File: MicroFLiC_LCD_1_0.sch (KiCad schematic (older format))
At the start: 14 parts, among them P1 CONN_01X01, P2 CONN_01X01, P3 CONN_01X16, Q1 BCX54-16, U1 MCP4728, U2 TLV2371

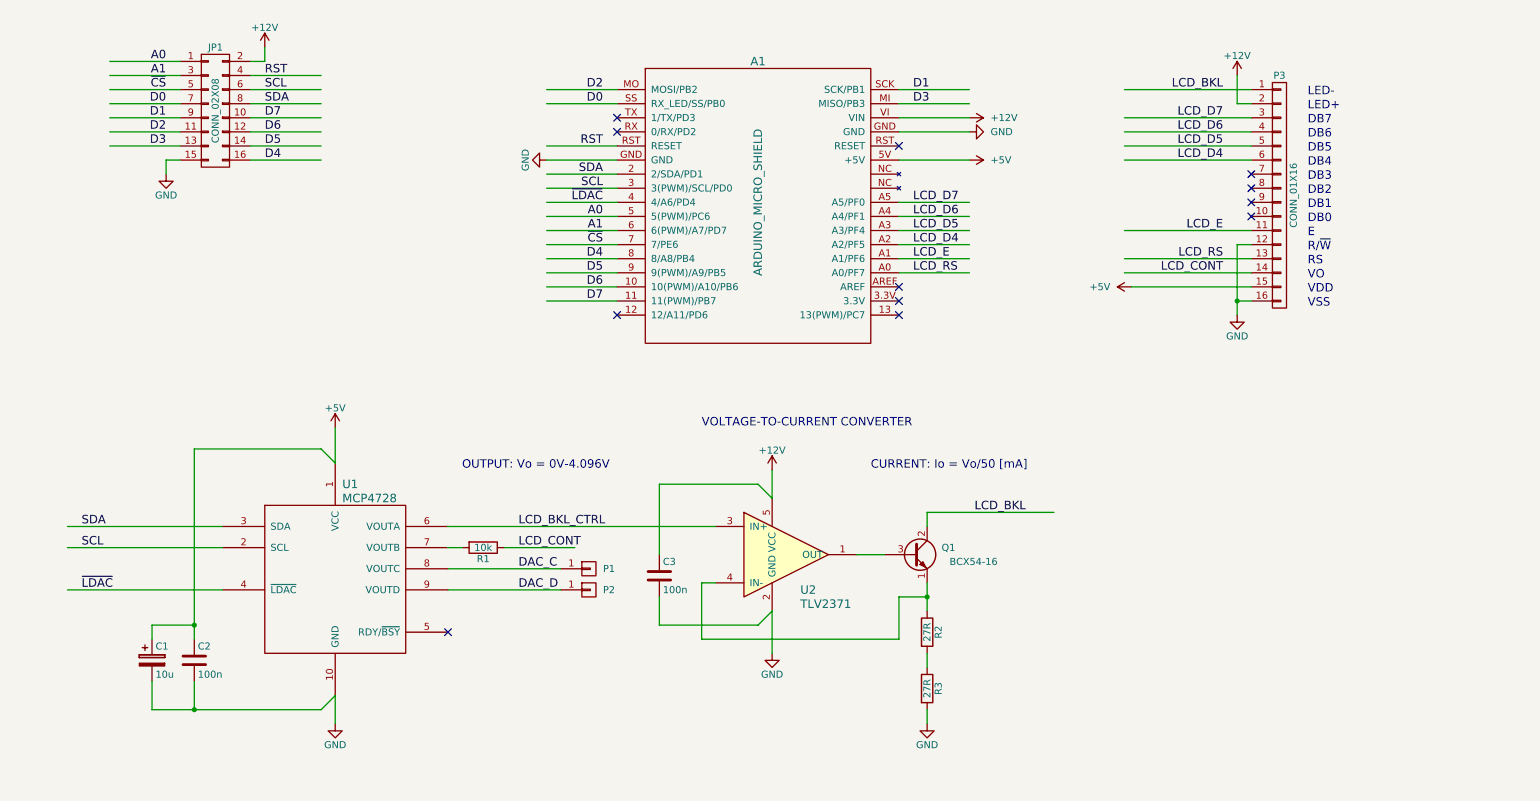
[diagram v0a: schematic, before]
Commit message: Created the PCB with 3D models
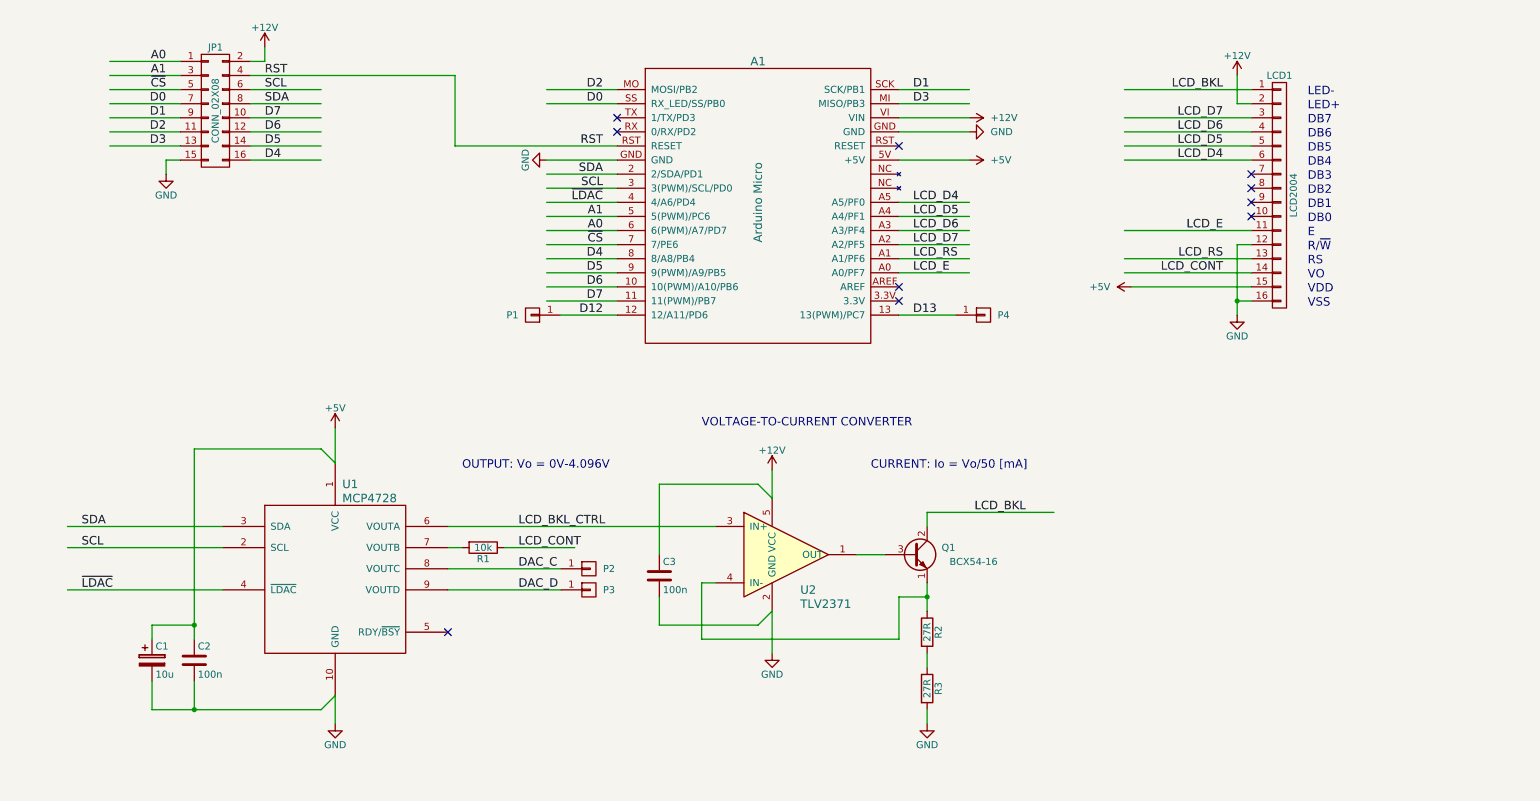
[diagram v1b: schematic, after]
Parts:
- added P1, P4: CONN_01X01, jakub:PIN_ARRAY_1, symbol CONN_01X01
- A1: value ARDUINO_MICRO_SHIELD -> Arduino Micro; footprint jakub:ARDUINO_MICRO_SHIELD -> jakub:ArduinoMicro
- JP1: footprint Socket_Strips:Socket_Strip_Straight_2x08 -> jakub:1-188275-6
- LCD1: renamed from P3; value CONN_01X16 -> LCD2004; footprint Socket_Strips:Socket_Strip_Straight_1x16 -> jakub:LCD2004
- Q1: footprint TO_SOT_Packages_SMD:SOT89-5_Housing -> TO_SOT_Packages_SMD:SOT89-3_Housing
- renumbered P1 to P2, P2 to P3
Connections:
- net labels added: D12, D13
- wire segments 95 -> 98
- no-connect marks 12 -> 10
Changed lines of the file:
@@
 P 6100 2300
 F 0 "A1" H 6100 3300 60  0000 C CNN
-F 1 "ARDUINO_MICRO_SHIELD" V 6100 2300 60  0000 C CNN
-F 2 "jakub:ARDUINO_MICRO_SHIELD" V 5350 2750 60  0001 C CNN
+F 1 "Arduino Micro" V 6100 2300 60  0000 C CNN
+F 2 "jakub:ArduinoMicro" V 5350 2750 60  0001 C CNN
 F 3 "" V 5350 2750 60  0000 C CNN
 	1    6100 2300
@@
 F 0 "JP1" H 2250 2100 50  0000 C CNN
 F 1 "CONN_02X08" V 2250 1650 50  0000 C CNN
-F 2 "Socket_Strips:Socket_Strip_Straight_2x08" H 2250 450 50  0001 C CNN
+F 2 "jakub:1-188275-6" H 2250 450 50  0001 C CNN
 F 3 "" H 2250 450 50  0000 C CNN
 	1    2250 1650
@@
 	2000 2000 1900 2000
 Wire Wire Line
-	3000 1400 2500 1400
+	2500 1400 3950 1400
 Text Label 2600 1400 0    60   ~ 0
 RST
@@
 $EndComp
 Wire Wire Line
-	5100 1900 4600 1900
+	3950 1900 5100 1900
 Text Label 5000 1900 2    60   ~ 0
 RST
@@
 D6
 Wire Wire Line
+	5100 2500 4600 2500
+Text Label 5000 2500 2    60   ~ 0
+A0
+Wire Wire Line
 	5100 2600 4600 2600
+Wire Wire Line
+	5100 2400 4600 2400
 Text Label 5000 2600 2    60   ~ 0
 ~CS
-Wire Wire Line
-	5100 2400 4600 2400
-Wire Wire Line
-	5100 2500 4600 2500
 Text Label 5000 2400 2    60   ~ 0
-A0
-Text Label 5000 2500 2    60   ~ 0
 A1
 NoConn ~ 5100 1700
@@
 NoConn ~ 7100 3000
 $Comp
-L CONN_01X16 P3
+L CONN_01X16 LCD1
 U 1 1 566ABBC7
 P 9800 2250
-F 0 "P3" H 9800 3100 50  0000 C CNN
-F 1 "CONN_01X16" V 9900 2250 50  0000 C CNN
-F 2 "Socket_Strips:Socket_Strip_Straight_1x16" H 9800 2250 50  0001 C CNN
+F 0 "LCD1" H 9800 3100 50  0000 C CNN
+F 1 "LCD2004" V 9900 2250 50  0000 C CNN
+F 2 "jakub:LCD2004" H 9800 2250 50  0001 C CNN
 F 3 "" H 9800 2250 50  0000 C CNN
 	1    9800 2250
@@
 	7600 2300 7100 2300
 Text Label 7200 2300 0    60   ~ 0
-LCD_D7
+LCD_D4
 Wire Wire Line
 	7600 2400 7100 2400
 Text Label 7200 2400 0    60   ~ 0
-LCD_D6
+LCD_D5
 Wire Wire Line
 	7600 2500 7100 2500
 Text Label 7200 2500 0    60   ~ 0
-LCD_D5
+LCD_D6
 Wire Wire Line
 	7600 2600 7100 2600
 Text Label 7200 2600 0    60   ~ 0
-LCD_D4
+LCD_D7
 NoConn ~ 9600 2100
 NoConn ~ 9600 2200
@@
 	7600 2700 7100 2700
 Text Label 7200 2700 0    60   ~ 0
-LCD_E
+LCD_RS
 Wire Wire Line
 	7600 2800 7100 2800
 Text Label 7200 2800 0    60   ~ 0
-LCD_RS
+LCD_E
 Wire Wire Line
 	5100 2300 4600 2300
 Text Label 5000 2300 2    60   ~ 0
 ~LDAC
-NoConn ~ 7100 3100
-NoConn ~ 5100 3100
 $Comp
 L MCP4728 U1
@@
 F 0 "Q1" H 7500 4850 50  0000 R CNN
 F 1 "BCX54-16" H 7800 4750 50  0000 R CNN
-F 2 "TO_SOT_Packages_SMD:SOT89-5_Housing" H 7400 4900 50  0001 C CNN
+F 2 "TO_SOT_Packages_SMD:SOT89-3_Housing" H 7400 4900 50  0001 C CNN
 F 3 "" H 7200 4800 50  0000 C CNN
 F 4 "BCX54-16" H 7200 4800 60  0001 C CNN "Part Number"
@@
 NoConn ~ 3900 5350
 $Comp
-L CONN_01X01 P1
+L CONN_01X01 P2
 U 1 1 566B2E28
 P 4900 4900
-F 0 "P1" H 5000 4900 50  0000 L CNN
+F 0 "P2" H 5000 4900 50  0000 L CNN
 F 1 "CONN_01X01" V 5000 4900 50  0001 C CNN
 F 2 "jakub:PIN_ARRAY_1" H 4900 4900 50  0001 C CNN
@@
 $EndComp
 $Comp
-L CONN_01X01 P2
+L CONN_01X01 P3
 U 1 1 566B2F00
 P 4900 5050
-F 0 "P2" H 5000 5050 50  0000 L CNN
+F 0 "P3" H 5000 5050 50  0000 L CNN
 F 1 "CONN_01X01" V 5000 5050 50  0001 C CNN
 F 2 "jakub:PIN_ARRAY_1" H 4900 5050 50  0001 C CNN
@@
 Text Notes 5700 3900 0    60   ~ 0
 VOLTAGE-TO-CURRENT CONVERTER
+$Comp
+L CONN_01X01 P4
+U 1 1 566C68B3
+P 7700 3100
+F 0 "P4" H 7800 3100 50  0000 L CNN
+F 1 "CONN_01X01" V 7800 3100 50  0001 C CNN
+F 2 "jakub:PIN_ARRAY_1" H 7700 3100 50  0001 C CNN
+F 3 "" H 7700 3100 50  0000 C CNN
+	1    7700 3100
+	1    0    0    -1
+$EndComp
+Wire Wire Line
+	7100 3100 7500 3100
+Text Label 7200 3100 0    60   ~ 0
+D13
+$Comp
+L CONN_01X01 P1
+U 1 1 566C6BE1
+P 4500 3100
+F 0 "P1" H 4600 3100 50  0000 L CNN
+F 1 "CONN_01X01" V 4600 3100 50  0001 C CNN
+F 2 "jakub:PIN_ARRAY_1" H 4500 3100 50  0001 C CNN
+F 3 "" H 4500 3100 50  0000 C CNN
+	1    4500 3100
+	-1   0    0    1
+$EndComp
+Wire Wire Line
+	4700 3100 5100 3100
+Text Label 5000 3100 2    60   ~ 0
+D12
+Wire Wire Line
+	3950 1400 3950 1900
 $EndSCHEMATC

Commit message: Final production board v1.0. Corrected LCD part v1.1
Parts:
- A1: Manufacturer (none) -> Arduino; Order Code (none) -> 2285194; Part Number (none) -> A000053
- C1: symbol CP -> C; Manufacturer (none) -> Murata; Order Code (none) -> 1828805; Part Number (none) -> GRM21BR61A106KE19L
- C2, C3: Manufacturer (none) -> Multicomp; Order Code (none) -> 1759166; Part Number (none) -> MC0805B104K250CT
- LCD1: Manufacturer (none) -> Midas; Order Code (none) -> 2483355; Part Number (none) -> MC42005A12W-VNMLR
- P1: renamed from JP1; value CONN_02X08 -> 2x8 pin header; footprint jakub:1-188275-6 -> Pin_Headers:Pin_Header_Straight_2x08; Manufacturer (none) -> Samtec; Order Code (none) -> 2254695; Part Number (none) -> HTSW-108-05-G-D
- Q1: Manufacturer (none) -> NXP
- R1: Manufacturer (none) -> Multicomp; Order Code (none) -> 2073607; Part Number (none) -> MCMR08X1002FTL
- R2, R3: value 27R -> 18R(0.25W); Manufacturer (none) -> Panasonic; Order Code (none) -> 2253864; Part Number (none) -> ERJP6WF18R0V
- U1: Manufacturer (none) -> Microchip
- U2: Manufacturer (none) -> Texas Instruments; Order Code 8544990 -> 8454990
- renumbered P1 to PP1, P2 to PP2, P3 to PP3, P4 to PP4
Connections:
- net labels added: A0_5V, A1_5V, D0_5V, D1_5V, D2_5V, D3_5V, D4_5V, D5_5V, D6_5V, D7_5V, ~CS_5V, ~RST, ~RST_5V
- net labels removed: RST
- wire segments 98 -> 122
- no-connect marks 10 -> 9
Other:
- note added: "20x4 alphanumeric LCD"
- note added: "Choose the values of resistors R2 and R3 for\nspecified maximum LCD backlight current (I)\n such that their total resistance (R) is:\nR = 4.096 / I."
- moved on the sheet: C2, P1, PP2, PP3, Q1, R1, R2, U1, U2

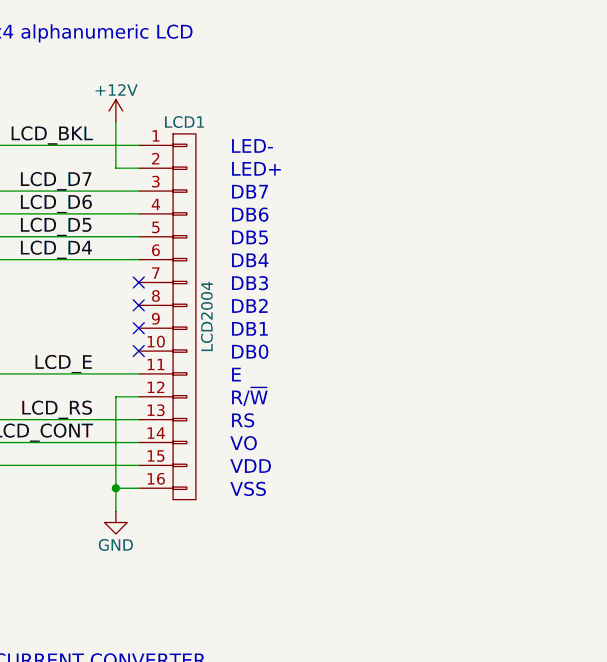
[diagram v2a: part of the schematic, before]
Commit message: Added connectors for LCD to the schematics
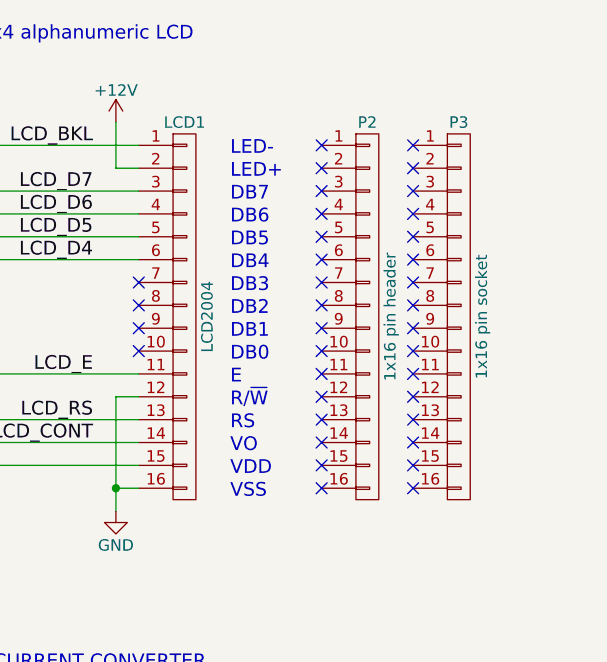
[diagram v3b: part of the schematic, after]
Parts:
- added P2: 1x16 pin header, symbol CONN_01X16
- added P3: 1x16 pin socket, symbol CONN_01X16
- P1: Alt. Order Code (none) -> 855-M20-9980845; Alt. Supplier (none) -> Mouser; Manufacturer Samtec -> Harwin; Note (none) -> 2x8 pin header; Order Code 2254695 -> 1022239; Package (none) -> DIL-16; Part Number HTSW-108-05-G-D -> M20-9980845; Supplier (none) -> Farnell
- U2: Order Code 8454990 -> 8454990
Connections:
- no-connect marks 9 -> 41
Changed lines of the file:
@@
 F 2 "Pin_Headers:Pin_Header_Straight_2x08" H 1550 850 50  0001 C CNN
 F 3 "" H 1550 850 50  0000 C CNN
-F 4 "HTSW-108-05-G-D" H 1550 2050 60  0001 C CNN "Part Number"
-F 5 "Samtec" H 1550 2050 60  0001 C CNN "Manufacturer"
-F 6 "2254695" H 1550 2050 60  0001 C CNN "Order Code"
+F 4 "M20-9980845" H 1550 2050 60  0001 C CNN "Part Number"
+F 5 "Harwin" H 1550 2050 60  0001 C CNN "Manufacturer"
+F 6 "DIL-16" H 1550 2050 60  0001 C CNN "Package"
+F 7 "Farnell" H 1550 2050 60  0001 C CNN "Supplier"
+F 8 "1022239" H 1550 2050 60  0001 C CNN "Order Code"
+F 9 "Mouser" H 1550 2050 60  0001 C CNN "Alt. Supplier"
+F 10 "855-M20-9980845" H 1550 2050 60  0001 C CNN "Alt. Order Code"
+F 11 "2x8 pin header" H 1550 2050 60  0001 C CNN "Note"
 	1    1550 2050
 	1    0    0    -1
@@
 F 4 "TLV2371IDBVT" H 9000 4700 60  0001 C CNN "Part Number"
 F 5 "Texas Instruments" H 9000 4700 60  0001 C CNN "Manufacturer"
-F 6 "8454990 " H 9000 4700 60  0001 C CNN "Order Code"
+F 6 "8454990" H 9000 4700 60  0001 C CNN "Order Code"
 	1    9000 4700
 	1    0    0    -1
@@
 Text Notes 8850 1050 0    60   ~ 0
 20x4 alphanumeric LCD
+$Comp
+L CONN_01X16 P2
+U 1 1 56C7B208
+P 10600 2250
+F 0 "P2" H 10600 3100 50  0000 C CNN
+F 1 "1x16 pin header" V 10700 2250 50  0000 C CNN
+F 2 "" H 10600 2250 50  0000 C CNN
+F 3 "" H 10600 2250 50  0000 C CNN
+F 4 "61301611121" H 10600 2250 60  0001 C CNN "Part Number"
+F 5 "Werth Elektronik" H 10600 2250 60  0001 C CNN "Manufacturer"
+F 6 "SIL-16" H 10600 2250 60  0001 C CNN "Package"
+F 7 "Farnell" H 10600 2250 60  0001 C CNN "Supplier"
+F 8 "2356166" H 10600 2250 60  0001 C CNN "Order Code"
+F 9 "Mouser" H 10600 2250 60  0001 C CNN "Alt. Supplier"
+F 10 "710-61301611121" H 10600 2250 60  0001 C CNN "Alt. Order Code"
+F 11 "1x16 header strip" H 10600 2250 60  0001 C CNN "Note"
+	1    10600 2250
+	1    0    0    -1
+$EndComp
+$Comp
+L CONN_01X16 P3
+U 1 1 56C7B356
+P 11000 2250
+F 0 "P3" H 11000 3100 50  0000 C CNN
+F 1 "1x16 pin socket" V 11100 2250 50  0000 C CNN
+F 2 "" H 11000 2250 50  0000 C CNN
+F 3 "" H 11000 2250 50  0000 C CNN
+F 4 "6-534237-4" H 11000 2250 60  0001 C CNN "Part Number"
+F 5 "TE Connectivity" H 11000 2250 60  0001 C CNN "Manufacturer"
+F 6 "SIL-16" H 11000 2250 60  0001 C CNN "Package"
+F 7 "Farnell" H 11000 2250 60  0001 C CNN "Supplier"
+F 8 "2311164" H 11000 2250 60  0001 C CNN "Order Code"
+F 9 "Mouser" H 11000 2250 60  0001 C CNN "Alt. Supplier"
+F 10 "571-6-534237-4" H 11000 2250 60  0001 C CNN "Alt. Order Code"
+F 11 "1x16 general socket strip" H 11000 2250 60  0001 C CNN "Note"
+	1    11000 2250
+	1    0    0    -1
+$EndComp
+NoConn ~ 10800 3000
+NoConn ~ 10800 2900
+NoConn ~ 10800 2800
+NoConn ~ 10800 2700
+NoConn ~ 10800 2600
+NoConn ~ 10800 2500
+NoConn ~ 10800 2400
+NoConn ~ 10800 2300
+NoConn ~ 10800 2200
+NoConn ~ 10800 2100
+NoConn ~ 10800 2000
+NoConn ~ 10800 1900
+NoConn ~ 10800 1800
+NoConn ~ 10800 1700
+NoConn ~ 10800 1600
+NoConn ~ 10800 1500
+NoConn ~ 10400 1500
+NoConn ~ 10400 1600
+NoConn ~ 10400 1700
+NoConn ~ 10400 1800
+NoConn ~ 10400 1900
+NoConn ~ 10400 2000
+NoConn ~ 10400 2100
+NoConn ~ 10400 2200
+NoConn ~ 10400 2300
+NoConn ~ 10400 2400
+NoConn ~ 10400 2500
+NoConn ~ 10400 2600
+NoConn ~ 10400 2700
+NoConn ~ 10400 2800
+NoConn ~ 10400 2900
+NoConn ~ 10400 3000
 $EndSCHEMATC
